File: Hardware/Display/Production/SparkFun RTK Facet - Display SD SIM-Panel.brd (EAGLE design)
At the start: 120.6 x 193.8 mm, 662 parts, among them J1 FPC_12_0.5MM_BACKFLIP, J10 FPC_12_0.5MM_BACKFLIP, J11 FPC_12_0.5MM_BACKFLIP, J12 microSD, J13 FPC_12_0.5MM_BACKFLIP, J14 FPC_12_0.5MM_BACKFLIP, J15 microSD, J16 microSD, J17 FPC_12_0.5MM_BACKFLIP, J18 FPC_12_0.5MM_BACKFLIP, J19 microSD, J2 microSD, J20 FPC_12_0.5MM_BACKFLIP, J21 FPC_12_0.5MM_BACKFLIP, J22 microSD, J23 FPC_12_0.5MM_BACKFLIP, J24 FPC_12_0.5MM_BACKFLIP, J25 microSD, J26 FPC_12_0.5MM_BACKFLIP, J27 FPC_12_0.5MM_BACKFLIP, J28 microSD, J29 FPC_12_0.5MM_BACKFLIP, J3 FPC_12_0.5MM_BACKFLIP, J30 FPC_12_0.5MM_BACKFLIP, J31 microSD, J32 FPC_12_0.5MM_BACKFLIP, J33 FPC_12_0.5MM_BACKFLIP, J34 microSD, J35 FPC_12_0.5MM_BACKFLIP, J36 FPC_12_0.5MM_BACKFLIP, J37 microSD, J38 FPC_12_0.5MM_BACKFLIP, J39 FPC_12_0.5MM_BACKFLIP, J4 FPC_12_0.5MM_BACKFLIP, J40 microSD, J41 FPC_12_0.5MM_BACKFLIP, J42 FPC_12_0.5MM_BACKFLIP, J43 microSD, J44 FPC_12_0.5MM_BACKFLIP, J45 FPC_12_0.5MM_BACKFLIP, J46 microSD, J47 FPC_12_0.5MM_BACKFLIP, J48 FPC_12_0.5MM_BACKFLIP, J5 FPC_12_0.5MM_BACKFLIP, J6 microSD, J7 FPC_12_0.5MM_BACKFLIP, J8 FPC_12_0.5MM_BACKFLIP, J9 microSD, U1 LIS2DH12, U10 LIS2DH12, U11 LIS2DH12, U12 LIS2DH12, U13 LIS2DH12, U14 LIS2DH12, U15 LIS2DH12, U16 LIS2DH12, U2 LIS2DH12, U3 LIS2DH12, U4 LIS2DH12, U5 LIS2DH12, U6 LIS2DH12, U7 LIS2DH12, U8 LIS2DH12, U9 LIS2DH12

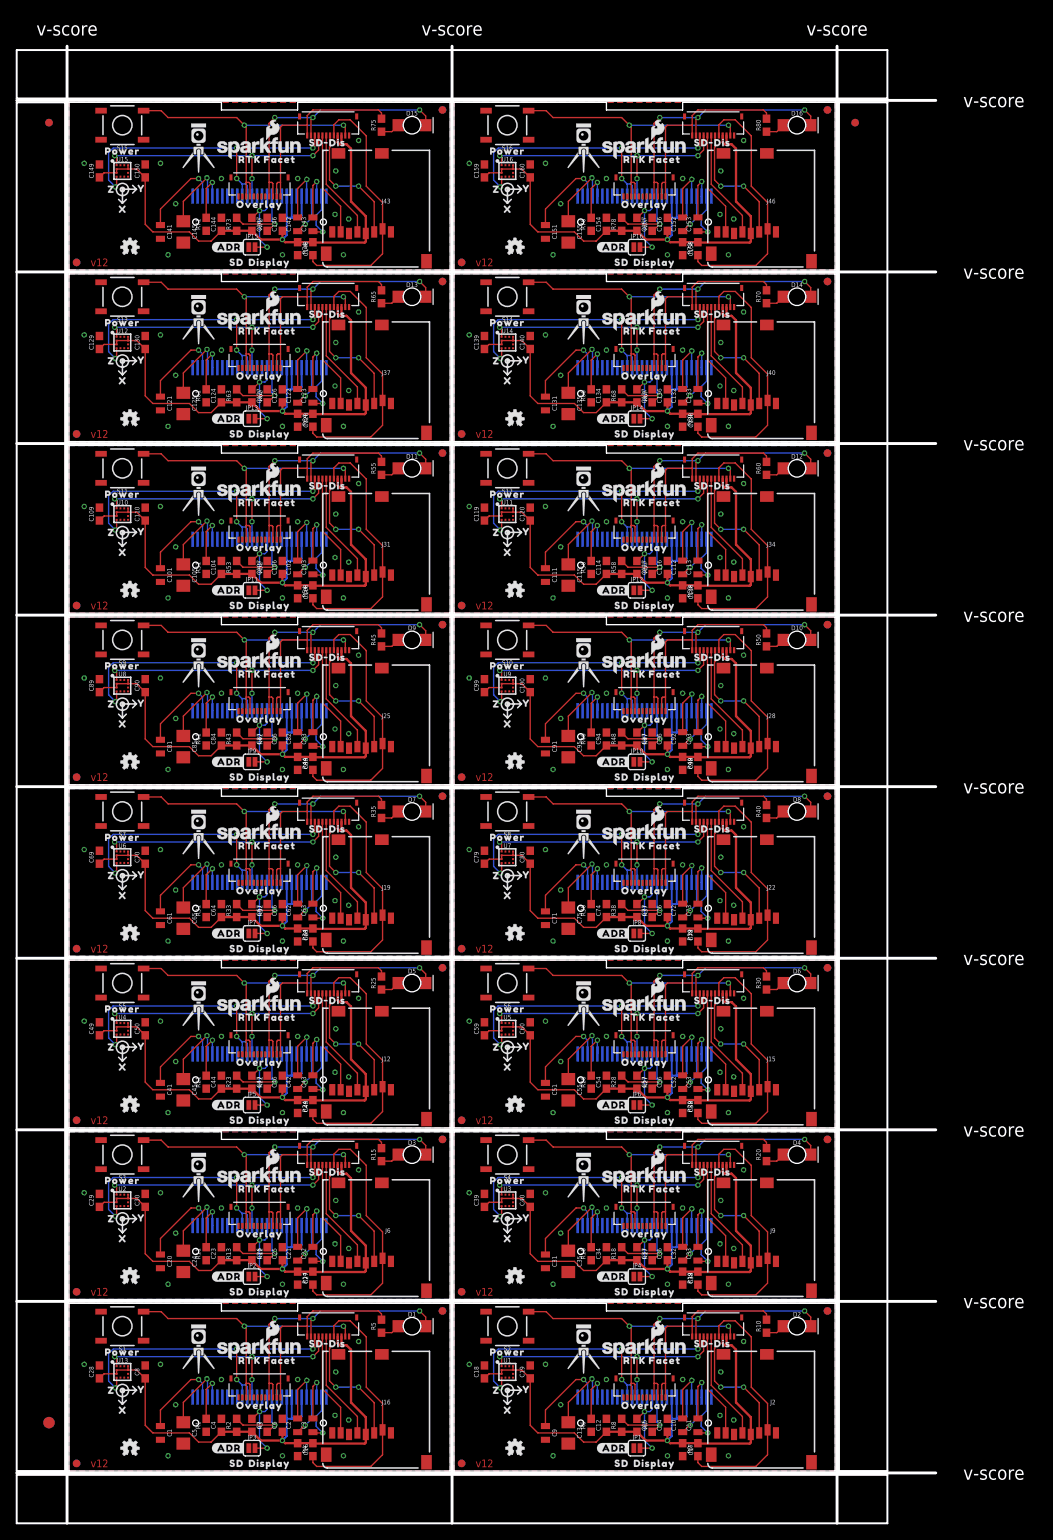
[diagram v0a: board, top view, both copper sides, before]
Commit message: Add production panel for Display v13 PCB.
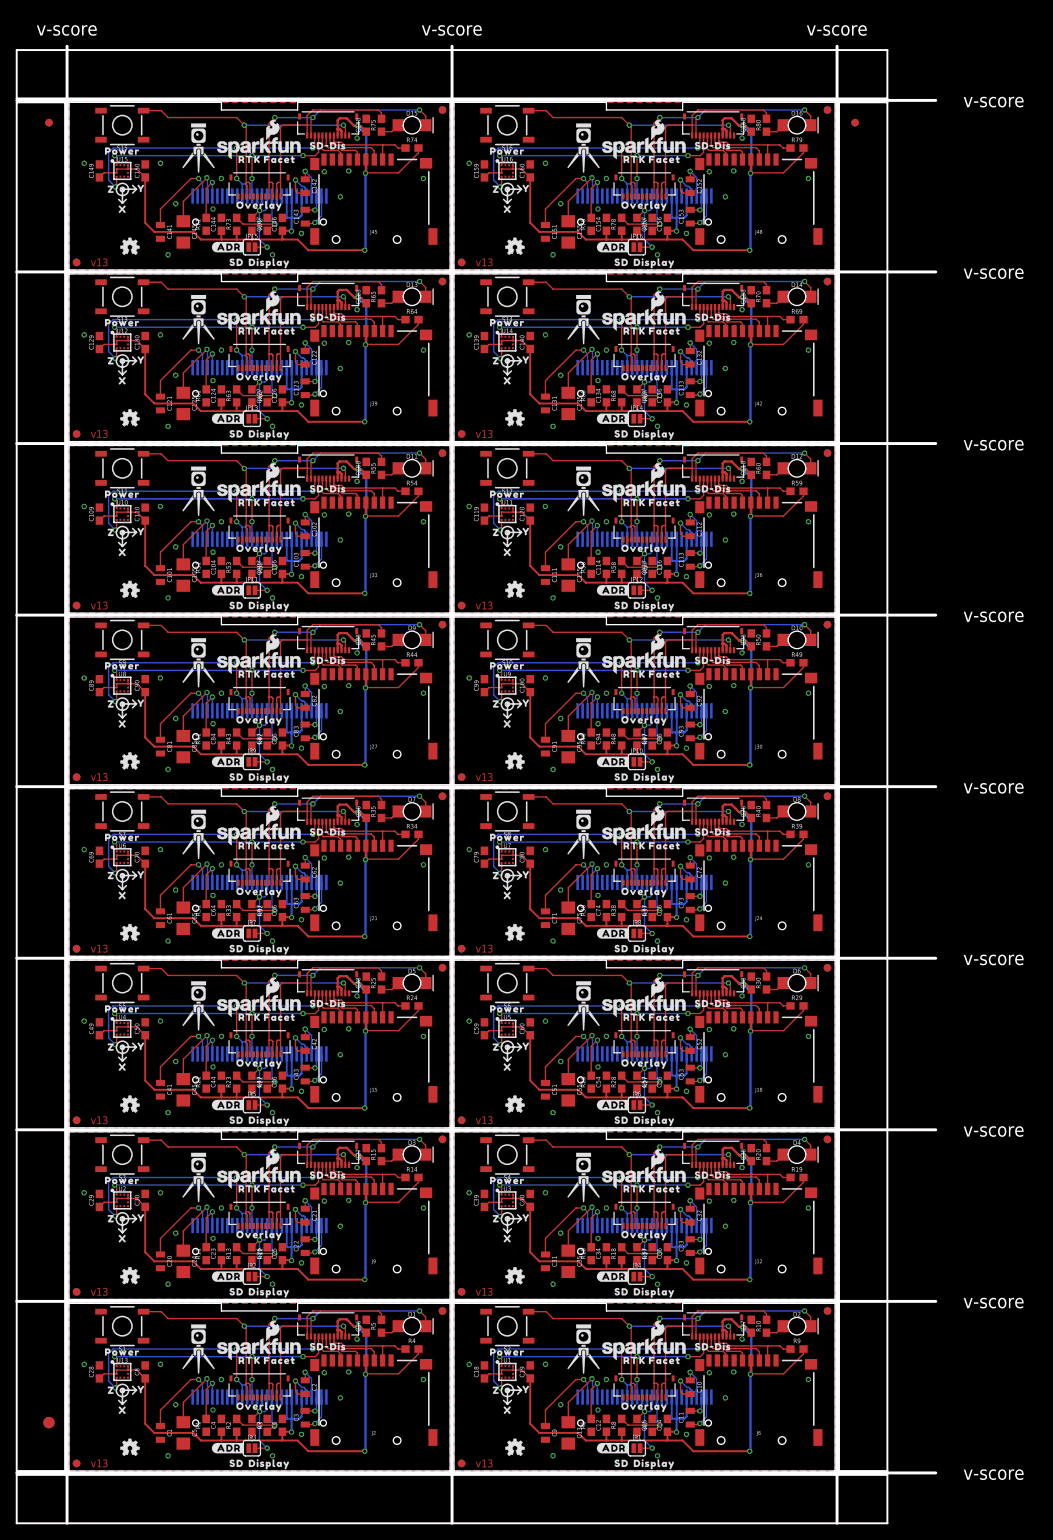
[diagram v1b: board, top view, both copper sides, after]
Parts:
- J12, J15, J2, J6, J9: value microSD -> MICRO-SD-PUSH-PUSH-EXT-PIN; device SparkFun-Connectors:MICRO-SD-SOCKET -> SparkFun-Connectors:MICROSD-EXTERNALPIN
- J16, J19, J22, J25, J28, J31, J34, J37, J40, J43, J46: value microSD -> FPC_12_0.5MM_BACKFLIP; device SparkFun-Connectors:MICRO-SD-SOCKET -> RTK Facet:FPC_12_DOUBLESIDED_BACKFLIP
- J18, J21, J24, J27, J30, J33, J36, J39, J42, J45, J48: value FPC_12_0.5MM_BACKFLIP -> MICRO-SD-PUSH-PUSH-EXT-PIN; device RTK Facet:FPC_12_DOUBLESIDED_BACKFLIP -> SparkFun-Connectors:MICROSD-EXTERNALPIN
- S1, S10, S11, S12, S13, S14, S15, S16, S2, S3, S4, S5, S6, S7, S8, S9: value (none) -> MOMENTARY-SWITCH-SPST-SMD-5.2MM-TALL
- moved J16 70.4 mm to (84.5, 64.0)
- moved J12 66.7 mm to (90.5, 26.5), turned to 0 degrees
- moved J6 66.7 mm to (90.5, 4.00), turned to 0 degrees
- moved J15 45.3 mm to (40.0, 49.0), turned to 0 degrees
- moved J2 45.3 mm to (40.0, 4.00), turned to 0 degrees
- moved J9 45.3 mm to (40.0, 26.5), turned to 0 degrees
- moved C108 18.5 mm to (39.0, 131.5), turned to 90 degrees
- moved C118 18.5 mm to (89.5, 131.5), turned to 90 degrees
- moved C48 18.5 mm to (39.0, 64.0), turned to 90 degrees
- moved C58 18.5 mm to (89.5, 64.0), turned to 90 degrees
- moved C68 18.5 mm to (39.0, 86.5), turned to 90 degrees
- moved C78 18.5 mm to (89.5, 86.5), turned to 90 degrees
- moved C88 18.5 mm to (39.0, 109.0), turned to 90 degrees
- moved C98 18.5 mm to (89.5, 109.0), turned to 90 degrees
- moved C16 18.5 mm to (39.0, 19.0), turned to 90 degrees
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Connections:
- net 3.3V: now also J2.4; no longer J16.VCC
- net 3.3V1: now also J6.4; no longer J2.VCC
- net 3.3V10: now also J31.3, J31.4, J33.4; no longer J31.VCC, J32.3, J32.4
- net 3.3V11: now also J34.3, J34.4, J36.4; no longer J34.VCC, J35.3, J35.4
- net 3.3V12: now also J37.3, J37.4, J39.4; no longer J37.VCC, J38.3, J38.4
- net 3.3V13: now also J40.3, J40.4, J42.4; no longer J40.VCC, J41.3, J41.4
- net 3.3V14: now also J43.3, J43.4, J45.4; no longer J43.VCC, J44.3, J44.4
- net 3.3V15: now also J46.3, J46.4, J48.4; no longer J46.VCC, J47.3, J47.4
- net 3.3V2: now also J9.4; no longer J6.VCC
- net 3.3V3: now also J12.4; no longer J9.VCC
- net 3.3V4: now also J15.4; no longer J12.VCC
- net 3.3V5: now also J16.3, J16.4, J18.4; no longer J15.VCC, J17.3, J17.4
- net 3.3V6: now also J19.3, J19.4, J21.4; no longer J19.VCC, J20.3, J20.4
- net 3.3V7: now also J22.3, J22.4, J24.4; no longer J22.VCC, J23.3, J23.4
- net 3.3V8: now also J25.3, J25.4, J27.4; no longer J25.VCC, J26.3, J26.4
- net 3.3V9: now also J28.3, J28.4, J30.4; no longer J28.VCC, J29.3, J29.4
- net CHARGE_LED10: now also J31.11, J32.3, J32.4; no longer J32.11, J33.3, J33.4
- net CHARGE_LED11: now also J34.11, J35.3, J35.4; no longer J35.11, J36.3, J36.4
- net CHARGE_LED12: now also J37.11, J38.3, J38.4; no longer J38.11, J39.3, J39.4
- net CHARGE_LED13: now also J40.11, J41.3, J41.4; no longer J41.11, J42.3, J42.4
- net CHARGE_LED14: now also J43.11, J44.3, J44.4; no longer J44.11, J45.3, J45.4
- net CHARGE_LED15: now also J46.11, J47.3, J47.4; no longer J47.11, J48.3, J48.4
- net CHARGE_LED5: now also J16.11, J17.3, J17.4; no longer J17.11, J18.3, J18.4
- net CHARGE_LED6: now also J19.11, J20.3, J20.4; no longer J20.11, J21.3, J21.4
- net CHARGE_LED7: now also J22.11, J23.3, J23.4; no longer J23.11, J24.3, J24.4
- net CHARGE_LED8: now also J25.11, J26.3, J26.4; no longer J26.11, J27.3, J27.4
- net CHARGE_LED9: now also J28.11, J29.3, J29.4; no longer J29.11, J30.3, J30.4
- net ESP_21/SDA10: now also J31.10; no longer J32.10
- net ESP_21/SDA11: now also J34.10; no longer J35.10
- net ESP_21/SDA12: now also J37.10; no longer J38.10
- net ESP_21/SDA13: now also J40.10; no longer J41.10
- net ESP_21/SDA14: now also J43.10; no longer J44.10
- net ESP_21/SDA15: now also J46.10; no longer J47.10
- net ESP_21/SDA5: now also J16.10; no longer J17.10
- net ESP_21/SDA6: now also J19.10; no longer J20.10
- net ESP_21/SDA7: now also J22.10; no longer J23.10
- net ESP_21/SDA8: now also J25.10; no longer J26.10
- net ESP_21/SDA9: now also J28.10; no longer J29.10
- net ESP_22/SCL10: now also J31.9; no longer J32.9
- net ESP_22/SCL11: now also J34.9; no longer J35.9
- net ESP_22/SCL12: now also J37.9; no longer J38.9
- net ESP_22/SCL13: now also J40.9; no longer J41.9
- net ESP_22/SCL14: now also J43.9; no longer J44.9
- net ESP_22/SCL15: now also J46.9; no longer J47.9
- net ESP_22/SCL5: now also J16.9; no longer J17.9
- net ESP_22/SCL6: now also J19.9; no longer J20.9
- net ESP_22/SCL7: now also J22.9; no longer J23.9
- net ESP_22/SCL8: now also J25.9; no longer J26.9
- net ESP_22/SCL9: now also J28.9; no longer J29.9
- net GND: now also J2.10, J2.11, J2.12, J2.13, J2.6, J2.9; no longer J16.CD1, J16.GND, J16.GND1, J16.GND3
- net GND1: now also J6.10, J6.11, J6.12, J6.13, J6.6, J6.9; no longer J2.CD1, J2.GND, J2.GND1, J2.GND3
- net GND10: now also J31.1, J32.11, J32.12, J33.10, J33.13, J33.6, J33.9; no longer J31.CD1, J31.GND, J31.GND1, J31.GND3, J32.1
- net GND11: now also J34.1, J35.11, J35.12, J36.10, J36.13, J36.6, J36.9; no longer J34.CD1, J34.GND, J34.GND1, J34.GND3, J35.1
- net GND12: now also J37.1, J38.11, J38.12, J39.10, J39.13, J39.6, J39.9; no longer J37.CD1, J37.GND, J37.GND1, J37.GND3, J38.1
- net GND13: now also J40.1, J41.11, J41.12, J42.10, J42.13, J42.6, J42.9; no longer J40.CD1, J40.GND, J40.GND1, J40.GND3, J41.1
- net GND14: now also J43.1, J44.11, J44.12, J45.10, J45.13, J45.6, J45.9; no longer J43.CD1, J43.GND, J43.GND1, J43.GND3, J44.1
- net GND15: now also J46.1, J47.11, J47.12, J48.10, J48.13, J48.6, J48.9; no longer J46.CD1, J46.GND, J46.GND1, J46.GND3, J47.1
- net GND2: now also J9.10, J9.11, J9.12, J9.13, J9.6, J9.9; no longer J6.CD1, J6.GND, J6.GND1, J6.GND3
- net GND3: now also J12.10, J12.11, J12.12, J12.13, J12.6, J12.9; no longer J9.CD1, J9.GND, J9.GND1, J9.GND3
- net GND4: now also J15.10, J15.11, J15.12, J15.13, J15.6, J15.9; no longer J12.CD1, J12.GND, J12.GND1, J12.GND3
- net GND5: now also J16.1, J17.11, J17.12, J18.10, J18.13, J18.6, J18.9; no longer J15.CD1, J15.GND, J15.GND1, J15.GND3, J17.1
- net GND6: now also J19.1, J20.11, J20.12, J21.10, J21.13, J21.6, J21.9; no longer J19.CD1, J19.GND, J19.GND1, J19.GND3, J20.1
- net GND7: now also J22.1, J23.11, J23.12, J24.10, J24.13, J24.6, J24.9; no longer J22.CD1, J22.GND, J22.GND1, J22.GND3, J23.1
- net GND8: now also J25.1, J26.11, J26.12, J27.10, J27.13, J27.6, J27.9; no longer J25.CD1, J25.GND, J25.GND1, J25.GND3, J26.1
- net GND9: now also J28.1, J29.11, J29.12, J30.10, J30.13, J30.6, J30.9; no longer J28.CD1, J28.GND, J28.GND1, J28.GND3, J29.1
- net POWER_BTN10: now also J31.2, J32.10, J32.9; no longer J32.2, J33.10, J33.9
- net POWER_BTN11: now also J34.2, J35.10, J35.9; no longer J35.2, J36.10, J36.9
- net POWER_BTN12: now also J37.2, J38.10, J38.9; no longer J38.2, J39.10, J39.9
- net POWER_BTN13: now also J40.2, J41.10, J41.9; no longer J41.2, J42.10, J42.9
- net POWER_BTN14: now also J43.2, J44.10, J44.9; no longer J44.2, J45.10, J45.9
- net POWER_BTN15: now also J46.2, J47.10, J47.9; no longer J47.2, J48.10, J48.9
- net POWER_BTN5: now also J16.2, J17.10, J17.9; no longer J17.2, J18.10, J18.9
- net POWER_BTN6: now also J19.2, J20.10, J20.9; no longer J20.2, J21.10, J21.9
- net POWER_BTN7: now also J22.2, J23.10, J23.9; no longer J23.2, J24.10, J24.9
- net POWER_BTN8: now also J25.2, J26.10, J26.9; no longer J26.2, J27.10, J27.9
- net POWER_BTN9: now also J28.2, J29.10, J29.9; no longer J29.2, J30.10, J30.9
- net SD_!CS!: now also J2.2; no longer J16.CS/DAT3
- net SD_!CS!1: now also J6.2; no longer J2.CS/DAT3
- net SD_!CS!10: now also J31.5, J33.2; no longer J31.CS/DAT3, J32.5
- net SD_!CS!11: now also J34.5, J36.2; no longer J34.CS/DAT3, J35.5
- net SD_!CS!12: now also J37.5, J39.2; no longer J37.CS/DAT3, J38.5
- net SD_!CS!13: now also J40.5, J42.2; no longer J40.CS/DAT3, J41.5
- net SD_!CS!14: now also J43.5, J45.2; no longer J43.CS/DAT3, J44.5
- net SD_!CS!15: now also J46.5, J48.2; no longer J46.CS/DAT3, J47.5
- net SD_!CS!2: now also J9.2; no longer J6.CS/DAT3
- net SD_!CS!3: now also J12.2; no longer J9.CS/DAT3
- net SD_!CS!4: now also J15.2; no longer J12.CS/DAT3
- net SD_!CS!5: now also J16.5, J18.2; no longer J15.CS/DAT3, J17.5
- net SD_!CS!6: now also J19.5, J21.2; no longer J19.CS/DAT3, J20.5
- net SD_!CS!7: now also J22.5, J24.2; no longer J22.CS/DAT3, J23.5
- net SD_!CS!8: now also J25.5, J27.2; no longer J25.CS/DAT3, J26.5
- net SD_!CS!9: now also J28.5, J30.2; no longer J28.CS/DAT3, J29.5
- net SD_CIPO: now also J2.7; no longer J16.DO/DAT0
- net SD_CIPO1: now also J6.7; no longer J2.DO/DAT0
- net SD_CIPO10: now also J31.8, J33.7; no longer J31.DO/DAT0, J32.8
- net SD_CIPO11: now also J34.8, J36.7; no longer J34.DO/DAT0, J35.8
- net SD_CIPO12: now also J37.8, J39.7; no longer J37.DO/DAT0, J38.8
- net SD_CIPO13: now also J40.8, J42.7; no longer J40.DO/DAT0, J41.8
- net SD_CIPO14: now also J43.8, J45.7; no longer J43.DO/DAT0, J44.8
- net SD_CIPO15: now also J46.8, J48.7; no longer J46.DO/DAT0, J47.8
- net SD_CIPO2: now also J9.7; no longer J6.DO/DAT0
- net SD_CIPO3: now also J12.7; no longer J9.DO/DAT0
- net SD_CIPO4: now also J15.7; no longer J12.DO/DAT0
- net SD_CIPO5: now also J16.8, J18.7; no longer J15.DO/DAT0, J17.8
- net SD_CIPO6: now also J19.8, J21.7; no longer J19.DO/DAT0, J20.8
- net SD_CIPO7: now also J22.8, J24.7; no longer J22.DO/DAT0, J23.8
- net SD_CIPO8: now also J25.8, J27.7; no longer J25.DO/DAT0, J26.8
- net SD_CIPO9: now also J28.8, J30.7; no longer J28.DO/DAT0, J29.8
- net SD_COPI: now also J2.3; no longer J16.DI/CMD
- net SD_COPI1: now also J6.3; no longer J2.DI/CMD
- net SD_COPI10: now also J31.6, J33.3; no longer J31.DI/CMD, J32.6
- net SD_COPI11: now also J34.6, J36.3; no longer J34.DI/CMD, J35.6
- net SD_COPI12: now also J37.6, J39.3; no longer J37.DI/CMD, J38.6
- net SD_COPI13: now also J40.6, J42.3; no longer J40.DI/CMD, J41.6
- net SD_COPI14: now also J43.6, J45.3; no longer J43.DI/CMD, J44.6
- net SD_COPI15: now also J46.6, J48.3; no longer J46.DI/CMD, J47.6
- net SD_COPI2: now also J9.3; no longer J6.DI/CMD
- net SD_COPI3: now also J12.3; no longer J9.DI/CMD
- net SD_COPI4: now also J15.3; no longer J12.DI/CMD
- net SD_COPI5: now also J16.6, J18.3; no longer J15.DI/CMD, J17.6
- net SD_COPI6: now also J19.6, J21.3; no longer J19.DI/CMD, J20.6
- net SD_COPI7: now also J22.6, J24.3; no longer J22.DI/CMD, J23.6
- net SD_COPI8: now also J25.6, J27.3; no longer J25.DI/CMD, J26.6
- net SD_COPI9: now also J28.6, J30.3; no longer J28.DI/CMD, J29.6
- net SD_SCK: now also J2.5; no longer J16.SCLK
- net SD_SCK1: now also J6.5; no longer J2.SCLK
- net SD_SCK10: now also J31.7, J33.5; no longer J31.SCLK, J32.7
- net SD_SCK11: now also J34.7, J36.5; no longer J34.SCLK, J35.7
- net SD_SCK12: now also J37.7, J39.5; no longer J37.SCLK, J38.7
- net SD_SCK13: now also J40.7, J42.5; no longer J40.SCLK, J41.7
- net SD_SCK14: now also J43.7, J45.5; no longer J43.SCLK, J44.7
- net SD_SCK15: now also J46.7, J48.5; no longer J46.SCLK, J47.7
- net SD_SCK2: now also J9.5; no longer J6.SCLK
- net SD_SCK3: now also J12.5; no longer J9.SCLK
- net SD_SCK4: now also J15.5; no longer J12.SCLK
- net SD_SCK5: now also J16.7, J18.5; no longer J15.SCLK, J17.7
- net SD_SCK6: now also J19.7, J21.5; no longer J19.SCLK, J20.7
- net SD_SCK7: now also J22.7, J24.5; no longer J22.SCLK, J23.7
- net SD_SCK8: now also J25.7, J27.5; no longer J25.SCLK, J26.7
- net SD_SCK9: now also J28.7, J30.5; no longer J28.SCLK, J29.7
- net V_USB10: now also J31.12, J32.1, J32.2; no longer J32.12, J33.1, J33.2
- net V_USB11: now also J34.12, J35.1, J35.2; no longer J35.12, J36.1, J36.2
- net V_USB12: now also J37.12, J38.1, J38.2; no longer J38.12, J39.1, J39.2
- net V_USB13: now also J40.12, J41.1, J41.2; no longer J41.12, J42.1, J42.2
- net V_USB14: now also J43.12, J44.1, J44.2; no longer J44.12, J45.1, J45.2
- net V_USB15: now also J46.12, J47.1, J47.2; no longer J47.12, J48.1, J48.2
- net V_USB5: now also J16.12, J17.1, J17.2; no longer J17.12, J18.1, J18.2
- net V_USB6: now also J19.12, J20.1, J20.2; no longer J20.12, J21.1, J21.2
- net V_USB7: now also J22.12, J23.1, J23.2; no longer J23.12, J24.1, J24.2
- net V_USB8: now also J25.12, J26.1, J26.2; no longer J26.12, J27.1, J27.2
- net V_USB9: now also J28.12, J29.1, J29.2; no longer J29.12, J30.1, J30.2
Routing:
- net SD_!CS!3: track 34.0 -> 12.4 mm
- net SD_!CS!2: track 34.0 -> 12.4 mm
- net SD_!CS!15: track 34.0 -> 12.4 mm
- net SD_!CS!5: track 34.0 -> 12.4 mm
- net SD_!CS!4: track 34.0 -> 12.4 mm
- net SD_!CS!14: track 34.0 -> 12.4 mm
- net SD_!CS!1: track 34.0 -> 12.4 mm
- net SD_!CS!: track 34.0 -> 12.4 mm
- net SD_!CS!9: track 34.0 -> 12.4 mm
- net SD_!CS!13: track 34.0 -> 12.4 mm
- net SD_!CS!8: track 34.0 -> 12.4 mm
- net SD_!CS!12: track 34.0 -> 12.4 mm
- net SD_!CS!7: track 34.0 -> 12.4 mm
- net SD_!CS!6: track 34.0 -> 12.4 mm
- net SD_!CS!11: track 34.0 -> 12.4 mm
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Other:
- board text added: "v13"
- board text removed: "v12"

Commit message: Reduce Main, Connector, Display, and Cell board widths by 1mm to allow for v-score protrusion.
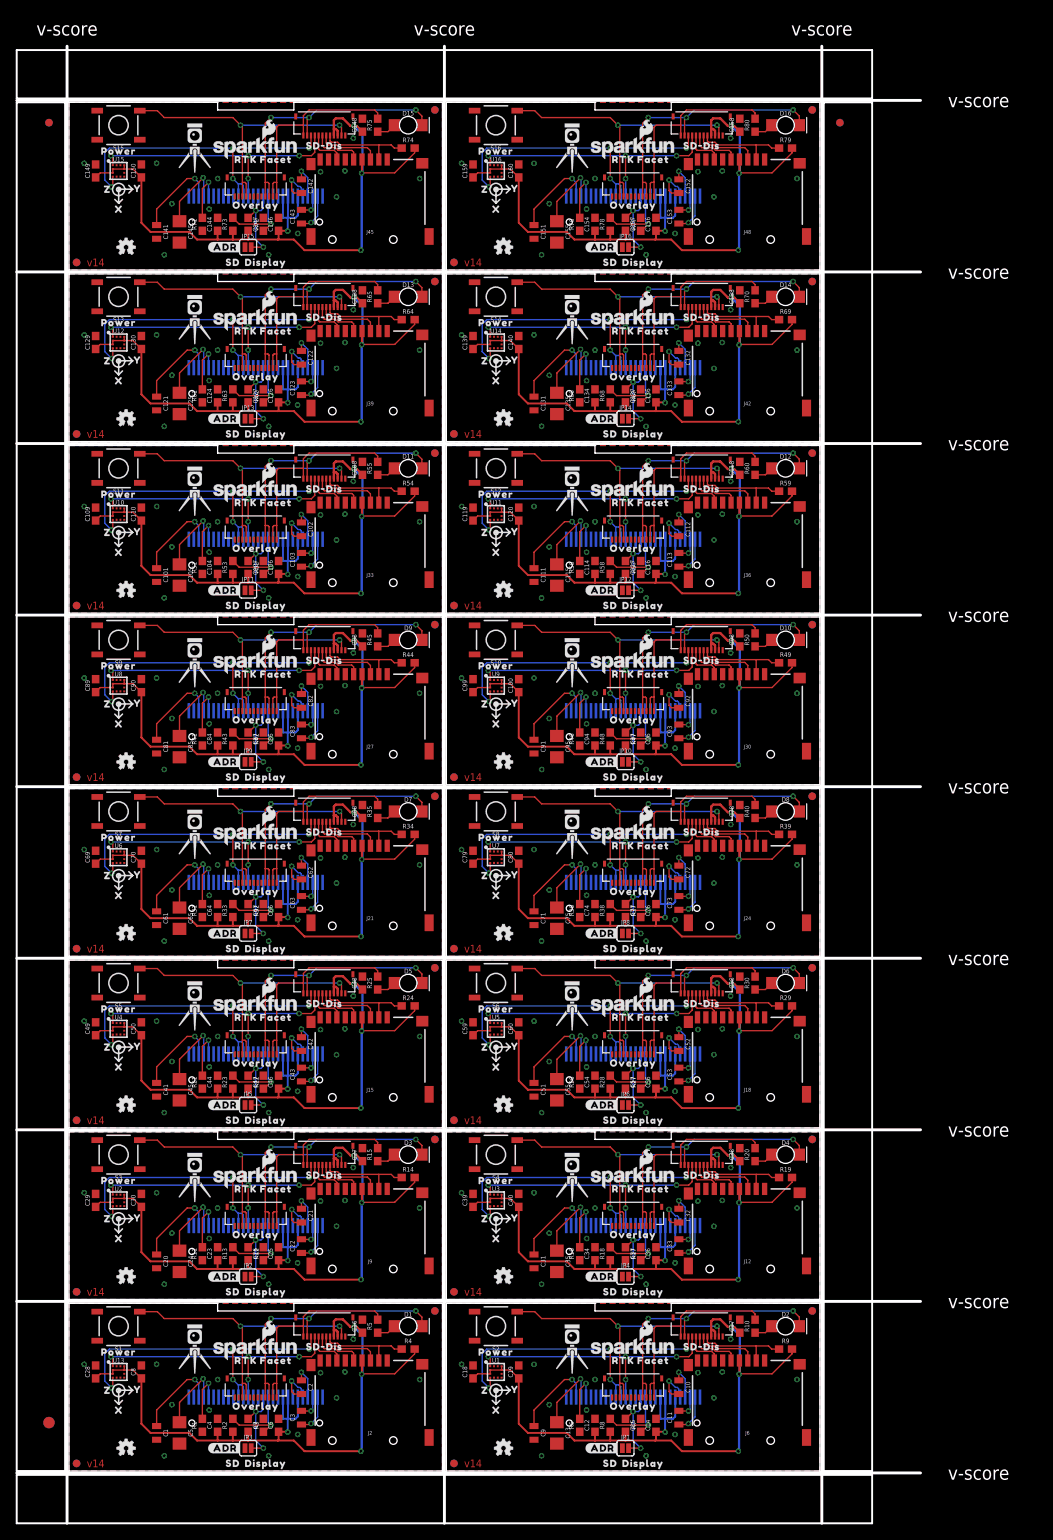
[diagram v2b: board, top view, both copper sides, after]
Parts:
- moved FID14 2.00 mm to (97.5, 43.5)
- moved FID15 2.00 mm to (97.5, 43.5)
- moved FID22 2.00 mm to (97.5, 66.0)
- moved FID23 2.00 mm to (97.5, 66.0)
- moved FID30 2.00 mm to (97.5, 88.5)
- moved FID31 2.00 mm to (97.5, 88.5)
- moved FID38 2.00 mm to (97.5, 111.0)
- moved FID39 2.00 mm to (97.5, 111.0)
- moved FID46 2.00 mm to (97.5, 133.5)
- moved FID47 2.00 mm to (97.5, 133.5)
- moved FID54 2.00 mm to (97.5, 156.0)
- moved FID55 2.00 mm to (97.5, 156.0)
- moved FID6 2.00 mm to (97.5, 21.0)
- moved FID62 2.00 mm to (97.5, 178.6)
- moved FID63 2.00 mm to (97.5, 178.6)
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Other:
- board size 120.6 x 193.8 mm -> 118.6 x 193.8 mm
- board text added: "v14"
- board text removed: "v13"
